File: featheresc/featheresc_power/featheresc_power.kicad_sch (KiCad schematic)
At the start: 17 parts, among them J1 VIN_GND, J2 VIN_POS, J7 interconnect1, J8 interconnect2

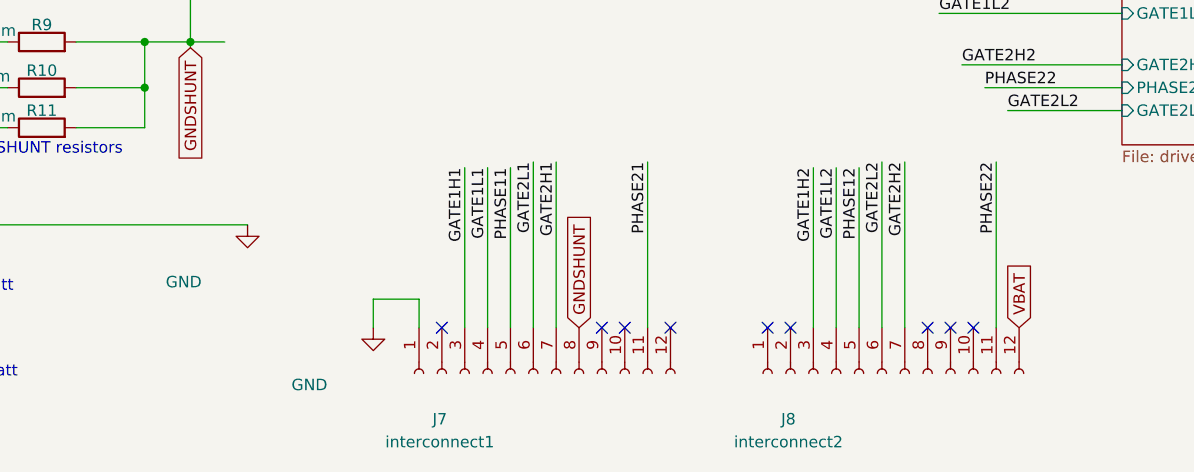
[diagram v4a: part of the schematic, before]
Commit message: improve interconnect pinouts
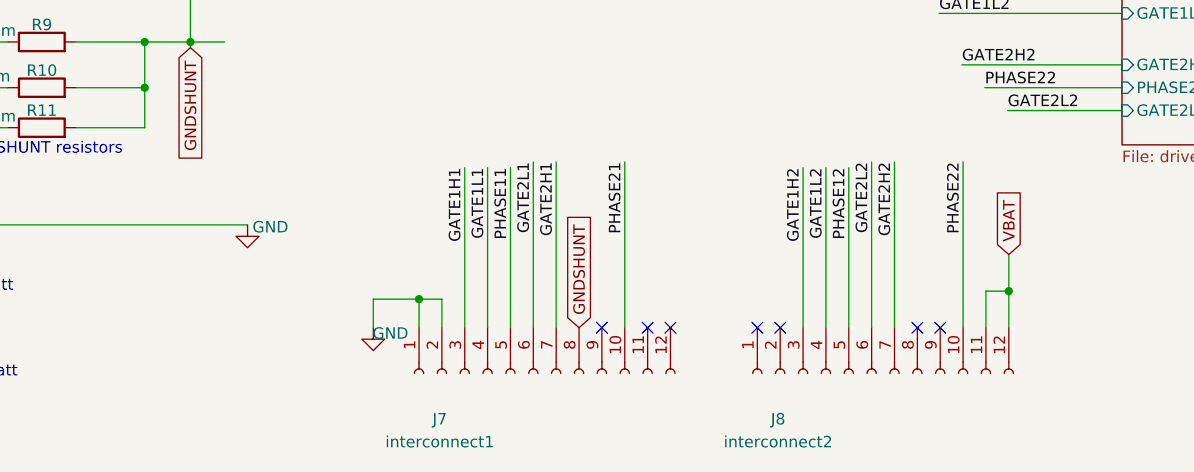
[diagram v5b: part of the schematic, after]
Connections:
- net GND: now also J7.2 (Pin_2)
- net PHASE21: now also J7.10 (Pin_10); no longer J7.11 (Pin_11)
- net PHASE22: now also J8.10 (Pin_10); no longer J8.11 (Pin_11)
- net VBAT: now also J8.11 (Pin_11)
- no-connect marks 9 -> 7
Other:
- moved on the sheet: J8
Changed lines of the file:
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@@
   (junction (at 82.55 76.835) (diameter 0) (color 0 0 0 0)
   )
+  (junction (at 205.232 129.286) (diameter 0) (color 0 0 0 0)
+  )
   (junction (at 114.3 101.6) (diameter 0) (color 0 0 0 0)
   )
@@
   (junction (at 80.645 106.68) (diameter 0) (color 0 0 0 0)
   )
+  (junction (at 139.7 130.175) (diameter 0) (color 0 0 0 0)
+  )
   (junction (at 110.49 76.835) (diameter 0) (color 0 0 0 0)
   )
-  (no_connect (at 142.24 133.35))
-  (no_connect (at 180.975 133.35))
-  (no_connect (at 196.215 133.35))
-  (no_connect (at 198.755 133.35))
-  (no_connect (at 201.295 133.35))
+  (no_connect (at 165.1 133.35))
+  (no_connect (at 179.832 133.35))
+  (no_connect (at 195.072 133.35))
+  (no_connect (at 197.612 133.35))
   (no_connect (at 160.02 133.35))
-  (no_connect (at 162.56 133.35))
   (no_connect (at 167.64 133.35))
-  (no_connect (at 178.435 133.35))
+  (no_connect (at 177.292 133.35))
+  (wire (pts (xy 202.692 133.35) (xy 202.692 129.286))
+    (stroke (width 0) (type default) (color 0 0 0 0))
+  )
   (wire (pts (xy 93.98 111.125) (xy 80.645 111.125))
     (stroke (width 0) (type default) (color 0 0 0 0))
@@
     (stroke (width 0) (type default) (color 0 0 0 0))
   )
-  (wire (pts (xy 191.135 114.935) (xy 191.135 133.35))
-    (stroke (width 0) (type default) (color 0 0 0 0))
-  )
-  (wire (pts (xy 193.675 114.935) (xy 193.675 133.35))
+  (wire (pts (xy 189.992 114.935) (xy 189.992 133.35))
+    (stroke (width 0) (type default) (color 0 0 0 0))
+  )
+  (wire (pts (xy 192.532 114.935) (xy 192.532 133.35))
     (stroke (width 0) (type default) (color 0 0 0 0))
   )
@@
     (stroke (width 0) (type default) (color 0 0 0 0))
   )
+  (wire (pts (xy 142.24 130.175) (xy 139.7 130.175))
+    (stroke (width 0) (type default) (color 0 0 0 0))
+  )
   (wire (pts (xy 147.32 54.61) (xy 170.18 54.61))
     (stroke (width 0) (type default) (color 0 0 0 0))
@@
     (stroke (width 0) (type default) (color 0 0 0 0))
   )
-  (wire (pts (xy 165.1 114.935) (xy 165.1 133.35))
+  (wire (pts (xy 162.56 114.935) (xy 162.56 133.35))
     (stroke (width 0) (type default) (color 0 0 0 0))
   )
@@
     (stroke (width 0) (type default) (color 0 0 0 0))
   )
-  (wire (pts (xy 186.055 115.57) (xy 186.055 133.35))
+  (wire (pts (xy 184.912 115.57) (xy 184.912 133.35))
     (stroke (width 0) (type default) (color 0 0 0 0))
   )
@@
     (stroke (width 0) (type default) (color 0 0 0 0))
   )
+  (wire (pts (xy 202.692 129.286) (xy 205.232 129.286))
+    (stroke (width 0) (type default) (color 0 0 0 0))
+  )
   (wire (pts (xy 192.405 93.345) (xy 217.805 93.345))
     (stroke (width 0) (type default) (color 0 0 0 0))
   )
-  (wire (pts (xy 203.835 114.935) (xy 203.835 133.35))
+  (wire (pts (xy 200.152 114.935) (xy 200.152 133.35))
     (stroke (width 0) (type default) (color 0 0 0 0))
   )
@@
     (stroke (width 0) (type default) (color 0 0 0 0))
   )
+  (wire (pts (xy 205.232 129.286) (xy 205.232 133.35))
+    (stroke (width 0) (type default) (color 0 0 0 0))
+  )
+  (wire (pts (xy 205.232 125.222) (xy 205.232 129.286))
+    (stroke (width 0) (type default) (color 0 0 0 0))
+  )
   (wire (pts (xy 101.6 101.6) (xy 109.22 101.6))
     (stroke (width 0) (type default) (color 0 0 0 0))
@@
     (stroke (width 0) (type default) (color 0 0 0 0))
   )
-  (wire (pts (xy 188.595 115.57) (xy 188.595 133.35))
+  (wire (pts (xy 142.24 133.35) (xy 142.24 130.175))
+    (stroke (width 0) (type default) (color 0 0 0 0))
+  )
+  (wire (pts (xy 187.452 115.57) (xy 187.452 133.35))
     (stroke (width 0) (type default) (color 0 0 0 0))
   )
@@
     (stroke (width 0) (type default) (color 0 0 0 0))
   )
-  (wire (pts (xy 183.515 115.57) (xy 183.515 133.35))
+  (wire (pts (xy 182.372 115.57) (xy 182.372 133.35))
     (stroke (width 0) (type default) (color 0 0 0 0))
   )
@@
     (effects (font (size 1.27 1.27)) (justify right bottom))
   )
-  (label "GATE1H2" (at 183.515 115.57 270)
+  (label "GATE1H2" (at 182.372 115.57 270)
     (effects (font (size 1.27 1.27)) (justify right bottom))
   )
@@
     (effects (font (size 1.27 1.27)) (justify left bottom))
   )
-  (label "PHASE21" (at 165.1 114.935 270)
+  (label "PHASE21" (at 162.56 114.935 270)
     (effects (font (size 1.27 1.27)) (justify right bottom))
   )
@@
     (effects (font (size 1.27 1.27)) (justify left bottom))
   )
-  (label "GATE1L2" (at 186.055 115.57 270)
+  (label "GATE1L2" (at 184.912 115.57 270)
     (effects (font (size 1.27 1.27)) (justify right bottom))
   )
@@
     (effects (font (size 1.27 1.27)) (justify left bottom))
   )
-  (label "GATE2H2" (at 193.675 114.935 270)
+  (label "GATE2H2" (at 192.532 114.935 270)
     (effects (font (size 1.27 1.27)) (justify right bottom))
   )
@@
     (effects (font (size 1.27 1.27)) (justify right bottom))
   )
-  (label "PHASE12" (at 188.595 115.57 270)
+  (label "PHASE12" (at 187.452 115.57 270)
     (effects (font (size 1.27 1.27)) (justify right bottom))
   )
@@
     (effects (font (size 1.27 1.27)) (justify right bottom))
   )
-  (label "PHASE22" (at 203.835 114.935 270)
+  (label "PHASE22" (at 200.152 114.935 270)
     (effects (font (size 1.27 1.27)) (justify right bottom))
   )
@@
     (effects (font (size 1.27 1.27)) (justify left bottom))
   )
-  (label "GATE2L2" (at 191.135 114.935 270)
-    (effects (font (size 1.27 1.27)) (justify right bottom))
-  )
-  (global_label "VBAT" (shape input) (at 206.375 133.35 90) (fields_autoplaced)
+  (label "GATE2L2" (at 189.992 114.935 270)
+    (effects (font (size 1.27 1.27)) (justify right bottom))
+  )
+  (global_label "VBAT" (shape input) (at 205.232 125.222 90) (fields_autoplaced)
     (effects (font (size 1.27 1.27)) (justify left))
-    (property "Intersheet References" "${INTERSHEET_REFS}" (id 0) (at 206.2956 126.5221 90)
+    (property "Intersheet References" "${INTERSHEET_REFS}" (id 0) (at 205.1526 118.3941 90)
       (effects (font (size 1.27 1.27)) (justify left) hide)
     )
@@
   )
   (symbol (lib_id "power:GND") (at 120.65 121.92 0) (unit 1)
-    (in_bom yes) (on_board yes) (fields_autoplaced)
+    (in_bom yes) (on_board yes)
     (property "Reference" "#PWR01" (id 0) (at 120.65 128.27 0)
       (effects (font (size 1.27 1.27)) hide)
     )
-    (property "Value" "GND" (id 1) (at 113.5553 128.27 0))
+    (property "Value" "GND" (id 1) (at 123.19 122.174 0))
     (property "Footprint" "" (id 2) (at 120.65 121.92 0)
       (effects (font (size 1.27 1.27)) hide)
@@
     (pin "2")
   )
-  (symbol (lib_id "Connector:Conn_01x12_Female") (at 191.135 138.43 90) (mirror x) (unit 1)
+  (symbol (lib_id "Connector:Conn_01x12_Female") (at 189.992 138.43 90) (mirror x) (unit 1)
     (in_bom yes) (on_board yes) (fields_autoplaced)
-    (property "Reference" "J8" (id 0) (at 180.7444 143.51 90))
-    (property "Value" "interconnect2" (id 1) (at 180.7444 146.05 90))
-    (property "Footprint" "Connector_PinSocket_2.54mm:PinSocket_1x12_P2.54mm_Vertical" (id 2) (at 191.135 138.43 0)
-      (effects (font (size 1.27 1.27)) hide)
-    )
-    (property "Datasheet" "~" (id 3) (at 191.135 138.43 0)
+    (property "Reference" "J8" (id 0) (at 179.6014 143.51 90))
+    (property "Value" "interconnect2" (id 1) (at 179.6014 146.05 90))
+    (property "Footprint" "Connector_PinSocket_2.54mm:PinSocket_1x12_P2.54mm_Vertical" (id 2) (at 189.992 138.43 0)
+      (effects (font (size 1.27 1.27)) hide)
+    )
+    (property "Datasheet" "~" (id 3) (at 189.992 138.43 0)
       (effects (font (size 1.27 1.27)) hide)
     )
@@
   )
   (symbol (lib_id "power:GND") (at 134.62 133.35 0) (unit 1)
-    (in_bom yes) (on_board yes) (fields_autoplaced)
+    (in_bom yes) (on_board yes)
     (property "Reference" "#PWR04" (id 0) (at 134.62 139.7 0)
       (effects (font (size 1.27 1.27)) hide)
     )
-    (property "Value" "GND" (id 1) (at 127.5253 139.7 0))
+    (property "Value" "GND" (id 1) (at 136.525 133.985 0))
     (property "Footprint" "" (id 2) (at 134.62 133.35 0)
       (effects (font (size 1.27 1.27)) hide)
